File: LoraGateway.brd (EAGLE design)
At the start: 124 x 42 mm, 150 parts, among them IC1 TPS7A80, P1 LTST-C191KGKT, P2 LTST-C930KGKT, P3 LTST-C930KGKT, U1 SC283, U10 SE2435L, U2 SC560H, U4 STM32F401CDU6, U6 SX1257, U7 SX1257, X1 USB2-MICRO, X2 MCU Prog Header, X3 END4825A, X4 END4263A, X5 SMA-KE11

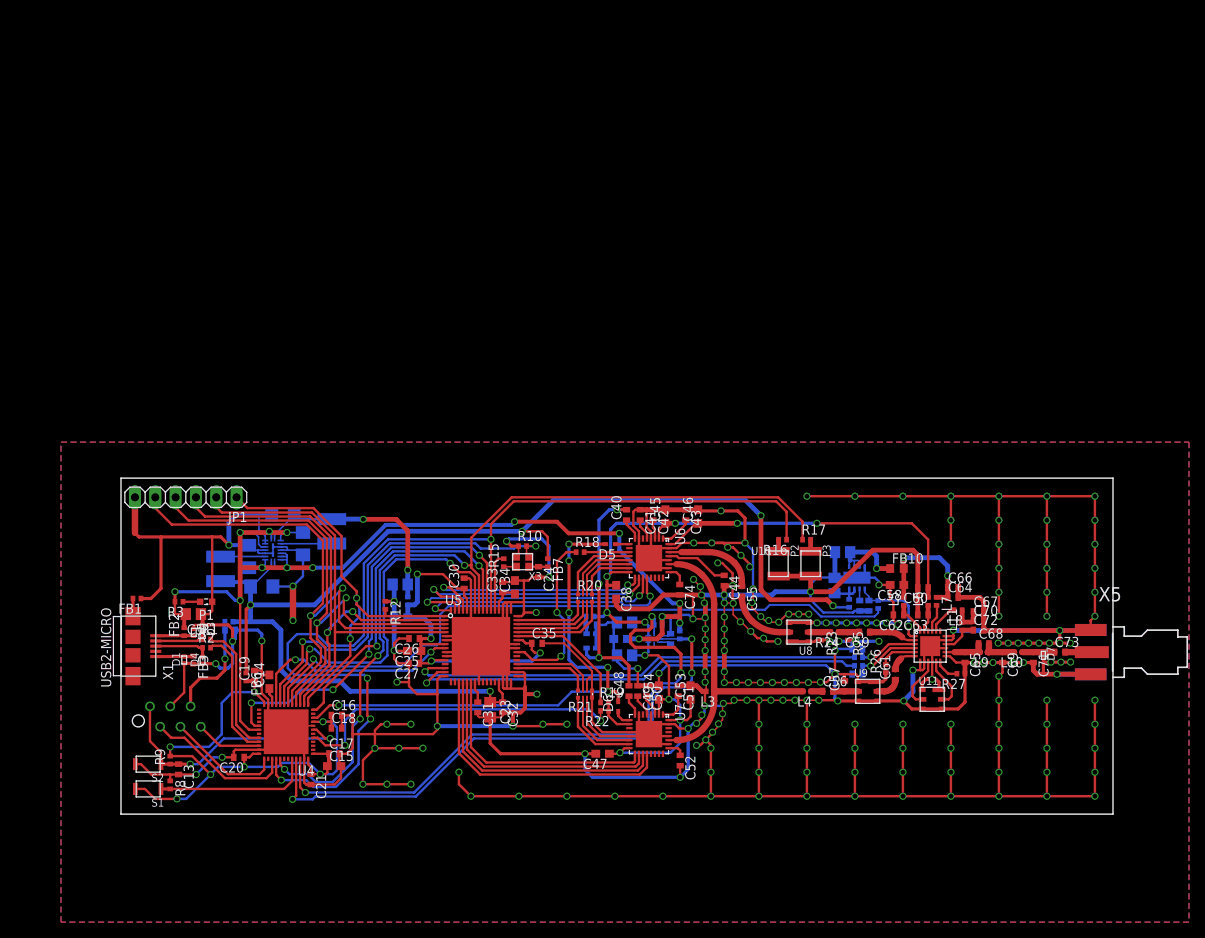
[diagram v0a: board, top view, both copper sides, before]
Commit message: old layout removed, Rpi-Zero Header added
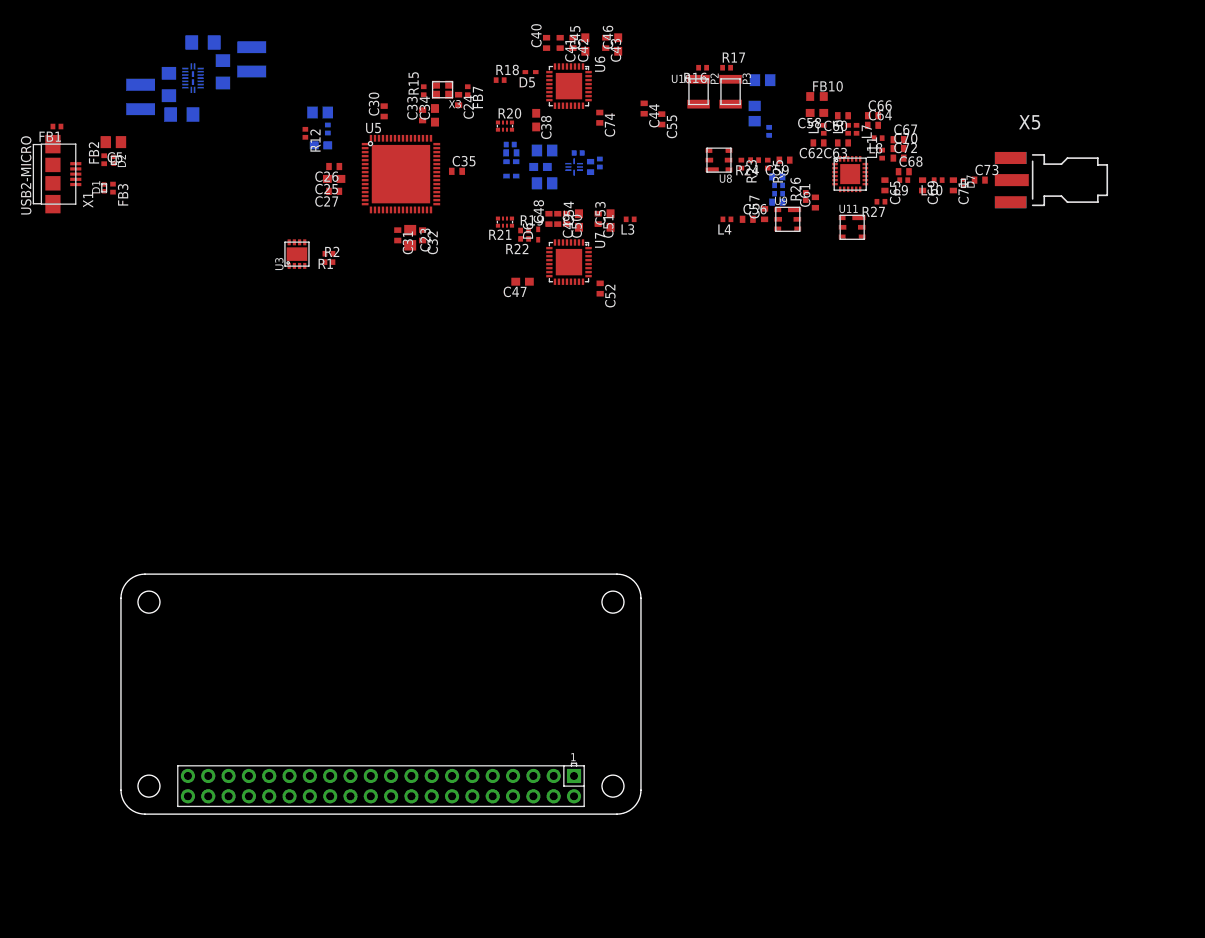
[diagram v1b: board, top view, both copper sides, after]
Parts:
- removed C12, C13, C17, C18, C19, C20, C21: 100nF, rcl:C0402
- removed C14, C15: 4.7µF, rcl:C0603
- removed C16: 1µF, rcl:C0402
- removed C22: 56pF, rcl:C0402
- removed C75: 10nF, rcl:C0402
- removed D3, D4: RCLAMP0531T, LoRa Gateway:SLP1006P2T
- removed FB5, FB6: (no value), LoRa Gateway:L0402
- removed IC1: TPS7A80, LoRa Gateway:SON-8
- removed JP1: SPI_Debug, pinhead:1X06
- removed P1: LTST-C191KGKT, LoRa Gateway:LED_SML0603
- removed R10: 10k, rcl:R0402
- removed R11: 100, rcl:R0402
- removed R3: 1k, rcl:R0402
- removed R8, R9: 100k, rcl:R0402
- removed S1, S2: KXT121LHS, LoRa Gateway:SMDSWITCH3.5X2.0MM
- removed U4: STM32F401CDU6, LoRa Gateway:P-QFP48-7X7MM
- removed X2: MCU Prog Header, con-amp-micromatch:MICROMATCH-6
- added J1: RPI-ZERO-HEADER, LoRa Gateway:RPI-ZERO
- added U3: (no value), LoRa Gateway:3X3MLPD-8
- R1: value 0R -> 16k
- R2: value 0R -> 12k
- moved C24 59.8 mm to (42.2, 89.3)
- moved C25 59.8 mm to (26.6, 79.4)
- moved C28 59.8 mm to (82.0, 79.7)
- moved C39 59.8 mm to (48.8, 82.7)
- moved C40 59.8 mm to (53.2, 96.4)
- moved C41 59.8 mm to (54.9, 96.4)
- moved C42 59.8 mm to (56.5, 96.4)
- moved C48 59.8 mm to (53.5, 74.4)
- moved C50 59.8 mm to (55.7, 74.4)
- moved C51 59.8 mm to (59.6, 74.4)
- moved C58 59.8 mm to (87.0, 87.7)
- moved C6 59.8 mm to (52.5, 80.9)
- moved C62 59.8 mm to (87.2, 83.9)
- moved C63 59.8 mm to (90.2, 83.9)
- moved C8 59.8 mm to (58.7, 80.9)
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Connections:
- removed net +3V3: C15.1, C16.1, C17.1, C18.1, C19.1, C20.1, C21.1, FB6.2, R9.2, S1.P$1, U4.1, U4.24, U4.36, U4.48, U4.9
- removed net BOOT0: R8.2, S1.P$2, U4.44
- removed net D+: D4.1, R2.1, X1.3
- removed net D-: D3.1, R1.1, X1.2
- removed net I2C1_SCL: U4.43
- removed net I2C1_SDA: U4.42
- removed net N$10: P1.A, R3.1
- removed net N$33: R11.2, U4.18
- removed net N$5: C12.1, FB5.1, X2.5
- removed net NRST: C13.1, R9.1, S2.P$2, U4.7, X2.1
- removed net RADIO2_RST: U4.31
- removed net SPI2_MISO: U4.27
- removed net SPI2_MOSI: U4.28
- removed net SPI2_NSS: U4.25
- removed net SPI2_SCK: U4.26
- removed net SWCLK: U4.37, X2.4
- removed net SWDIO: U4.34, X2.6
- removed net TRACESWO: U4.39, X2.2
- removed net USB_DM: R1.2, U4.32
- removed net USB_DP: R2.2, U4.33
- removed net VCAP: C14.1, U4.22
- net +5V: no longer R3.2, U4.30
- net 133M_OUT_EN: no longer R10.2, U4.20
- net CLKO_B_32M: no longer U4.5
- net FEM_EN: now also U3.2; no longer C22.1, IC1.5, R11.1
- net GND: now also R2.1, U3.8, U3.GND; no longer C12.2, C13.2, C14.2, C15.2, C16.2, C17.2, C18.2, C19.2, C20.2, C21.2, C22.2, C75.2, D3.2, D4.2, IC1.4, IC1.EXP, JP1.6, P1.C, R10.1, R8.1, S2.P$1, U4.23, U4.35, U4.47, U4.8, U4.EXP, X2.3
- net GPIO0: no longer U4.19
- net GPIO2: no longer U4.12
- net GPIO3: no longer U4.29
- net N$12: now also U3.3; no longer IC1.7, IC1.8
- net N$3: now also R1.1, R2.2, U3.7; no longer C75.1, IC1.6
- net PPS: no longer U4.21
- net RADIO_EN_A: no longer U4.45
- net RADIO_EN_B: no longer U4.46
- net RADIO_RST: no longer U4.10
- net RESET: no longer JP1.1, U4.13
- net RX_ON: no longer U4.41
- net SPI_MISO: no longer JP1.4, U4.16
- net SPI_MOSI: no longer JP1.5, U4.17
- net SPI_NSS: no longer JP1.2, U4.14
- net SPI_SCK: no longer JP1.3, U4.15
- net TX_ON: no longer U4.40
- net VCCDIG33: no longer FB5.2, FB6.1
- net VCCINT: now also R1.2, U3.6; no longer IC1.1, IC1.2, IC1.3
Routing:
- net GND: track 1207.0 -> 0.00 mm, vias 207 -> 0
- net VCCDIG33: track 163.3 -> 0.00 mm, vias 5 -> 0
- net +5V: track 142.4 -> 0.00 mm, vias 14 -> 0
- net TX_ON: track 129.4 -> 0.00 mm, vias 4 -> 0
- net RX_ON: track 106.7 -> 0.00 mm, vias 4 -> 0
- net VCCA_A: track 86.5 -> 0.00 mm, vias 6 -> 0
- net N$33: track 84.9 -> 0.00 mm, vias 1 -> 0
- net +3V3: track 79.0 -> 0.00 mm, vias 7 -> 0
- net RADIO_EN_B: track 76.7 -> 0.00 mm, vias 3 -> 0
- net RADIO_EN_A: track 72.4 -> 0.00 mm, vias 3 -> 0
- net SPI_MOSI: track 70.6 -> 0.00 mm, vias 2 -> 0
- net RADIO_RST: track 67.8 -> 0.00 mm, vias 6 -> 0
- net SPI_MISO: track 65.3 -> 0.00 mm, vias 2 -> 0
- net SPI_SCK: track 58.8 -> 0.00 mm, vias 2 -> 0
- net N$29: track 57.7 -> 0.00 mm, vias 1 -> 0
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- removed copper zone on layer 1, net GND
- removed copper zone on layer 16, net GND
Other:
- board size 124 x 42 mm -> 65 x 30 mm
